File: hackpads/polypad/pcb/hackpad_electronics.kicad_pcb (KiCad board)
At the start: 2 copper layers, 46.4 x 83.8 mm, 8 parts, among them J1 Conn_01x04_Pin, SW1 SW_Push, SW2 SW_Push, SW3 SW_Push, SW4 SW_Push, SW5 SW_Push, SW7 RotaryEncoder_Switch, U1 MOUDLE-SEEEDUINO-XIAO

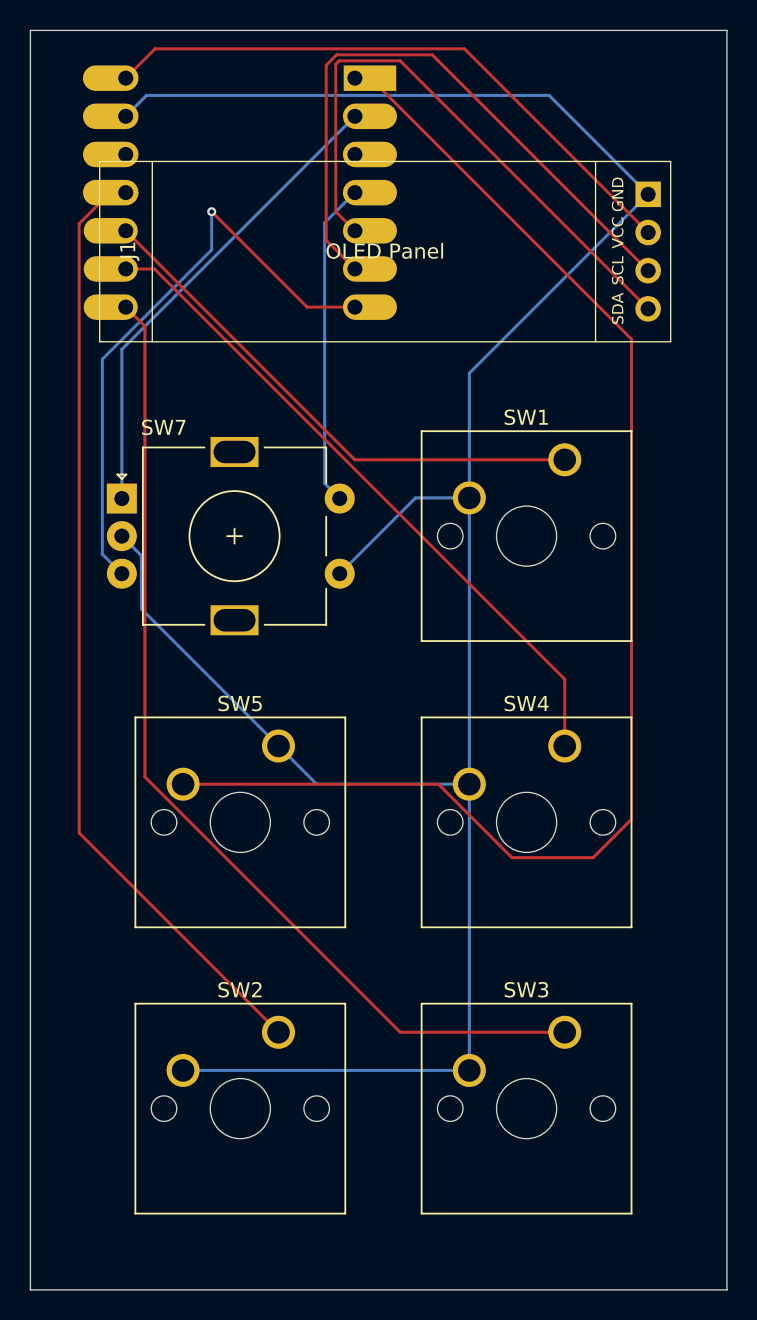
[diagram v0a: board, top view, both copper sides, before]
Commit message: clean up pcb silkscreen and corners
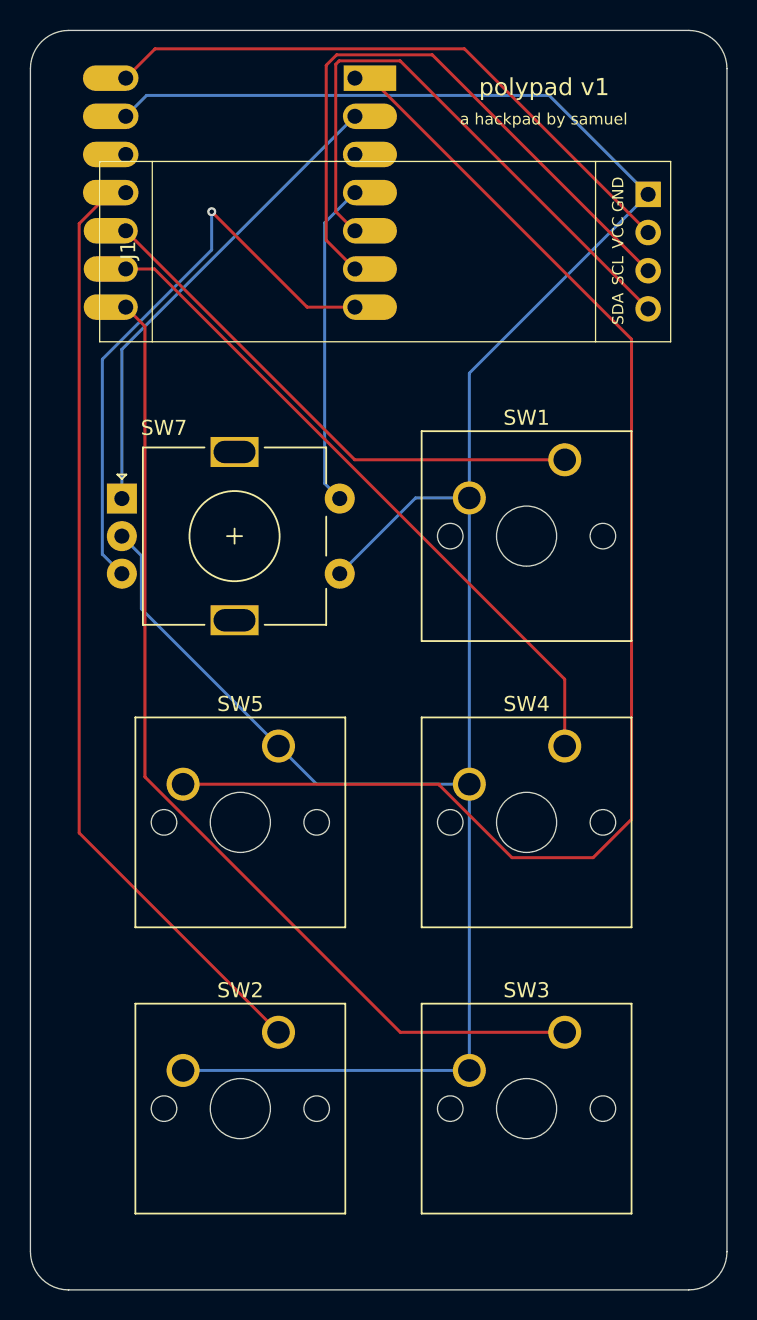
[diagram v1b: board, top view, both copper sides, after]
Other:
- outline, holes or cut-outs redrawn
- board text added: "a hackpad by samuel"
- board text added: "polypad v1"
